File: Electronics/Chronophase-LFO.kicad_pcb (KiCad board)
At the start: 2 copper layers, 29.2 x 101.6 mm, 68 parts, among them J1 CLK In, J5 Eurorack Connector, J7 BP_Inv_Out, J8 UP_Out, J9 BP_Out, U3 TL072, U4 TL072

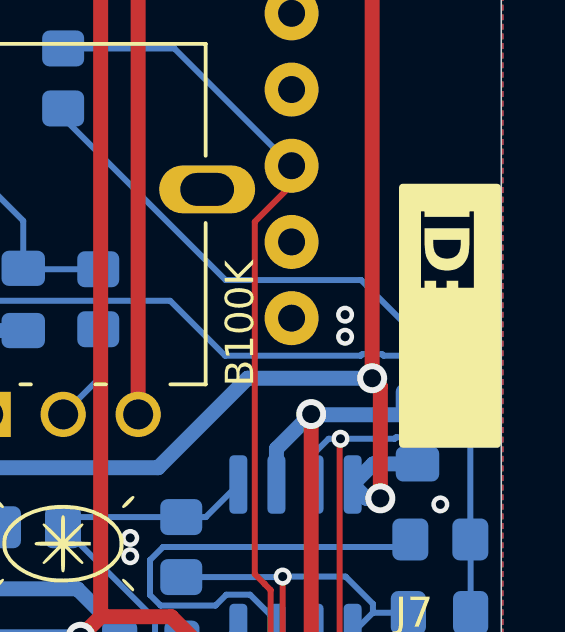
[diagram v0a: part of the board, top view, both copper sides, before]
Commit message: Updating to KiCad 10
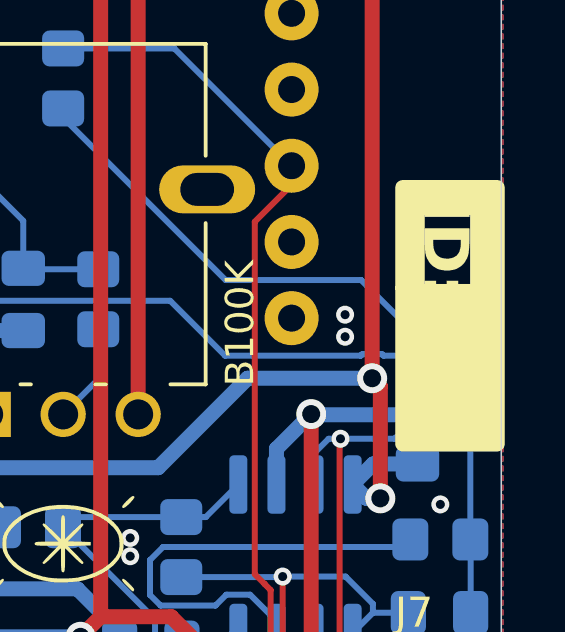
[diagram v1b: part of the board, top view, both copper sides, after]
